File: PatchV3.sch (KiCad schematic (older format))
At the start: 28 parts, among them J1 Conn_01x05, J2 2908-05WB-MG, U1 STM32WB5MMGH6TR_1-

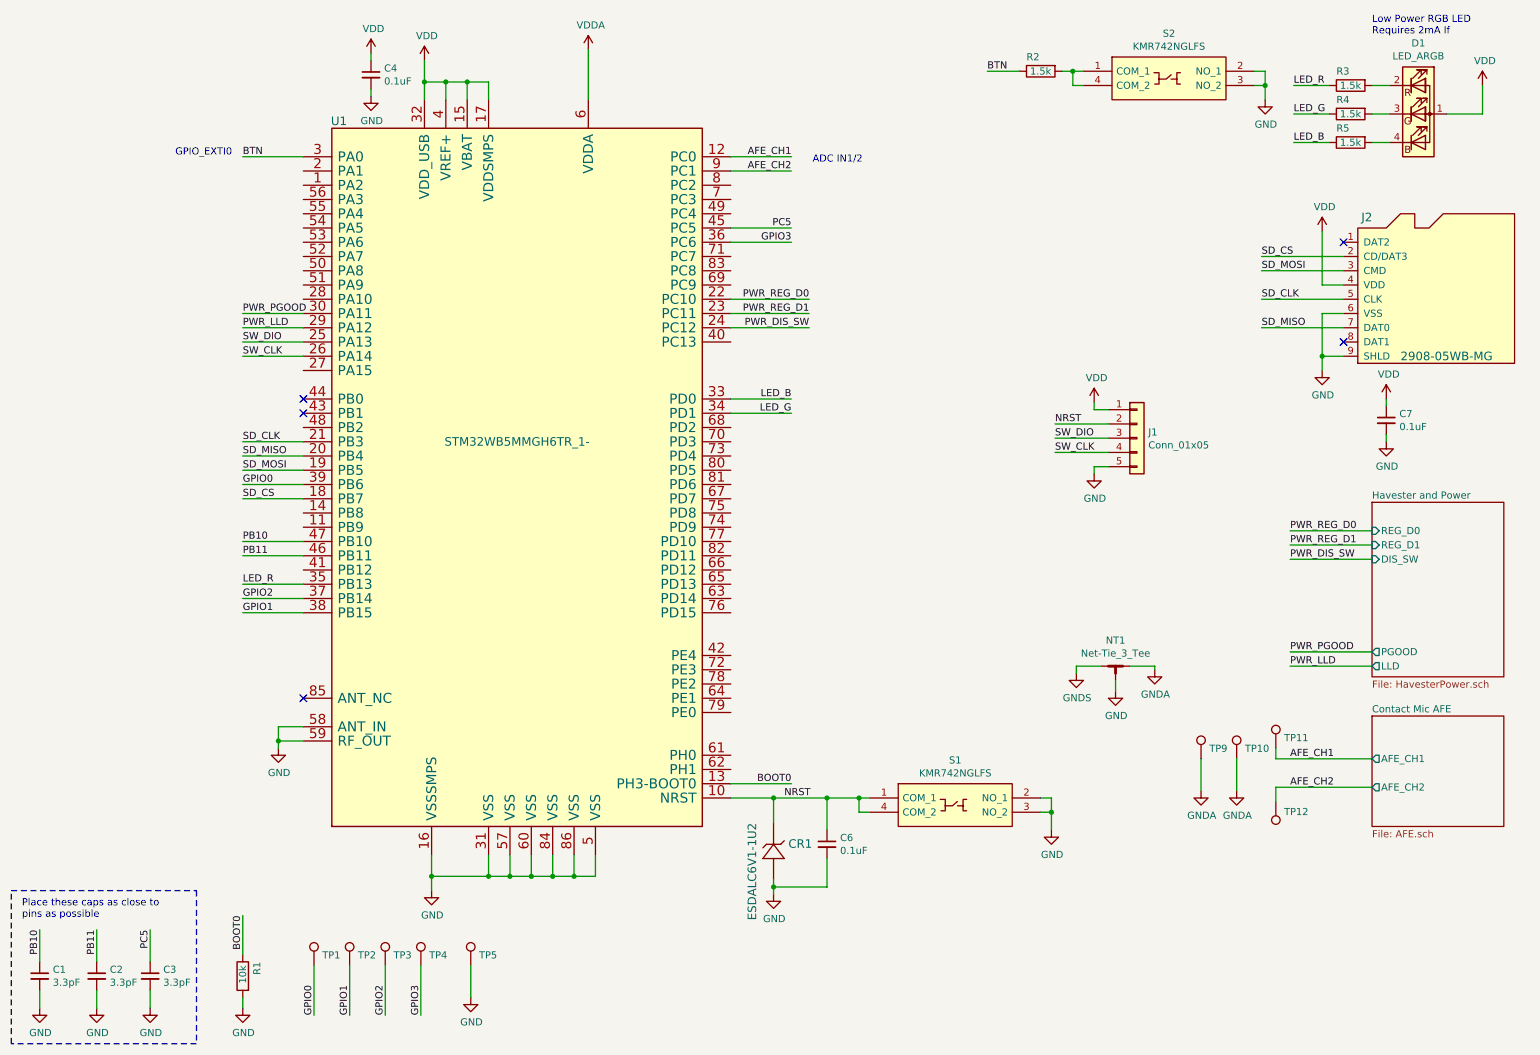
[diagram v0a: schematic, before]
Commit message: redid power section with new energy harverster ic
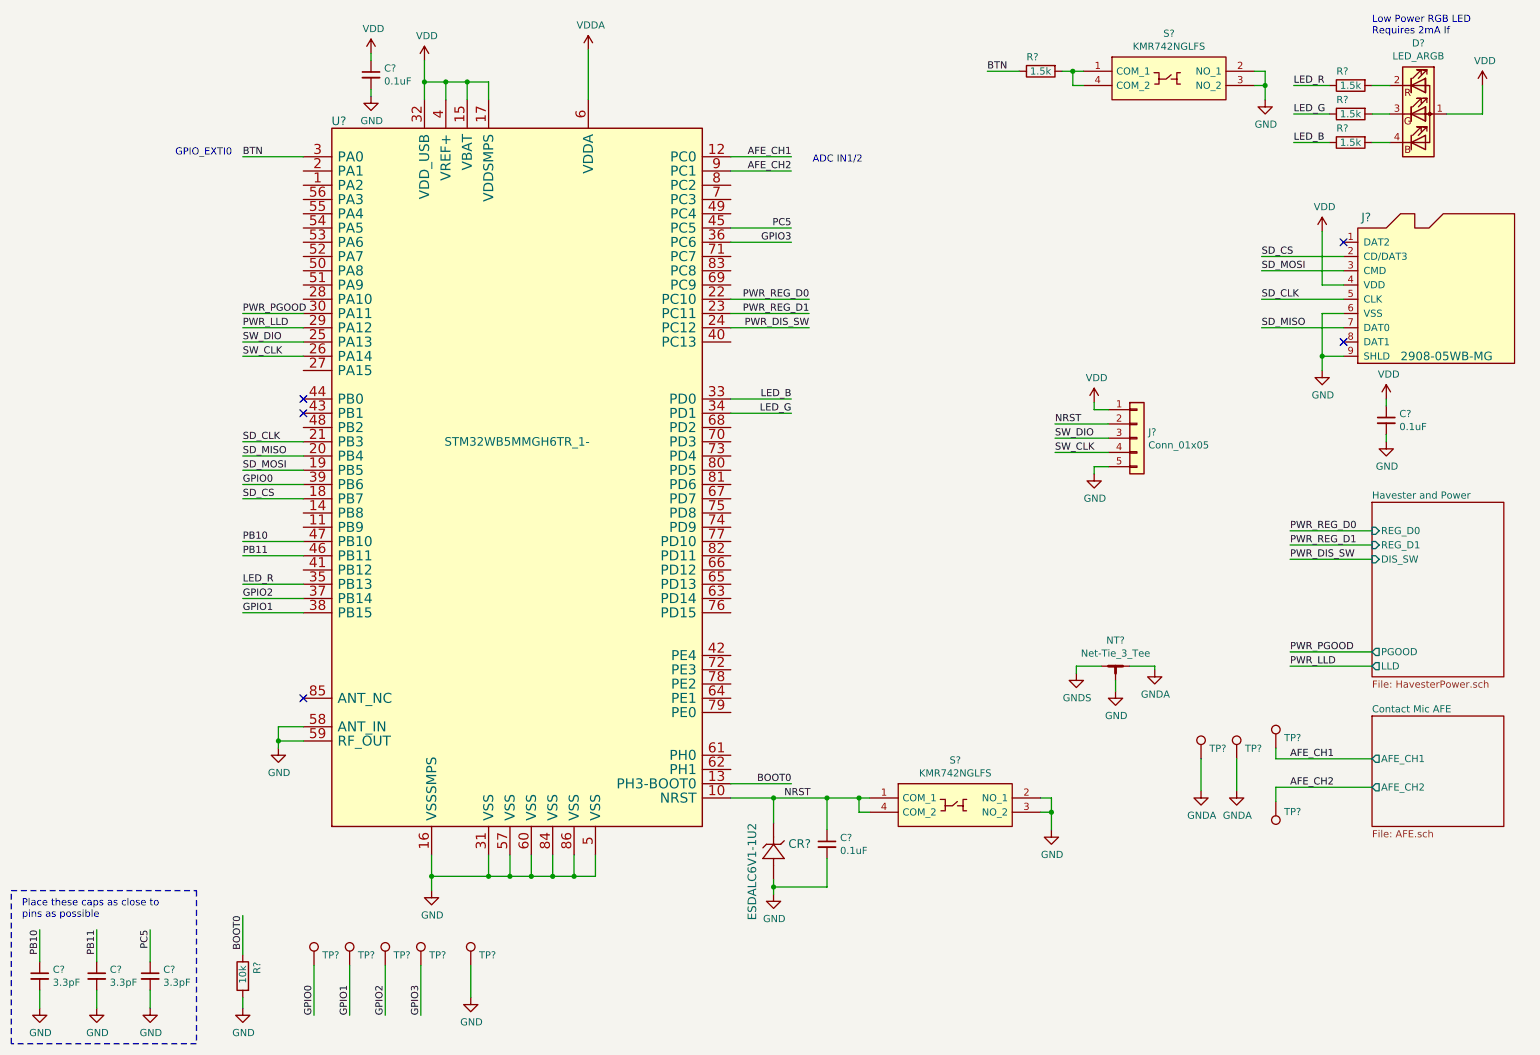
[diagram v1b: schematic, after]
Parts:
- renumbered C7 to C?, C6 to C?, C4 to C?, C1 to C?, C2 to C?, C3 to C?, CR1 to CR?, D1 to D?, J2 to J?, J1 to J?, NT1 to NT?, R3 to R?, R4 to R?, R5 to R?, R2 to R?, R1 to R?, S1 to S?, S2 to S?, TP1 to TP?, TP12 to TP?, TP2 to TP?, TP3 to TP?, TP4 to TP?, TP11 to TP?, TP5 to TP?, TP9 to TP?, TP10 to TP?, U1 to U?

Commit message: catch up
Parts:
- removed C? (x3): 3.3pF, Capacitor_SMD:C_0201_0603Metric, symbol Device:C_Small
- removed NT?: Net-Tie_3_Tee, PatchV2:gnd_tie, symbol Device:Net-Tie_3_Tee
- removed R?: 10k, Resistor_SMD:R_0402_1005Metric, symbol Device:R
- removed TP? (x4): TestPoint, TestPoint:TestPoint_Pad_1.5x1.5mm, symbol Connector:TestPoint
- removed U?: STM32WB5MMGH6TR_1-, PatchV2:SiP-LGA86, symbol PatchV2:STM32WB5MMGH6TR_1-
- added J?: Conn_02x04_Counter_Clockwise, symbol Connector_Generic:Conn_02x04_Counter_Clockwise
- added U?: LoRa-E5, PatchV2:LoRa-E5, symbol PatchV2:LoRa-E5
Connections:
- net labels added: LPUART_RX, LPUART_TX, ~BATT_CHG, ~BATT_CONN
- net labels removed: BOOT0, GNDS, PC5, VDDA
- wire segments 135 -> 109
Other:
- note added: "GPIO_EXTI5"
- note removed: "Place these caps as close to \npins as possible"
- moved on the sheet: C?, CR?, S?

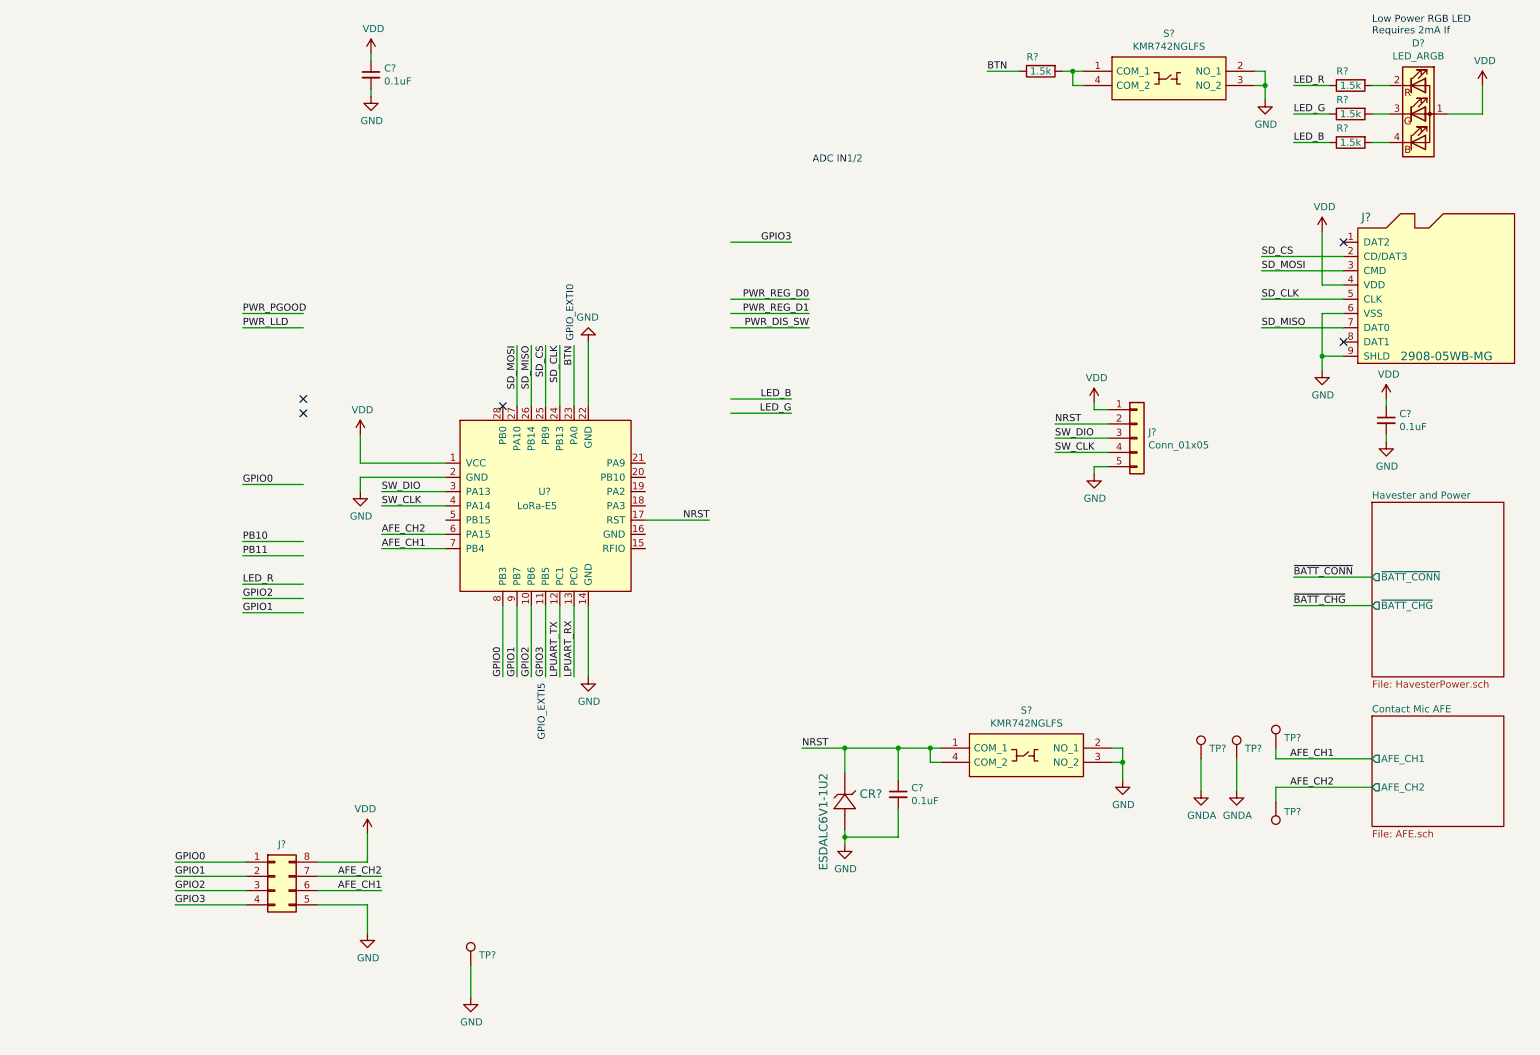
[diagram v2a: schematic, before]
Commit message: schematic functionally finished working on layout
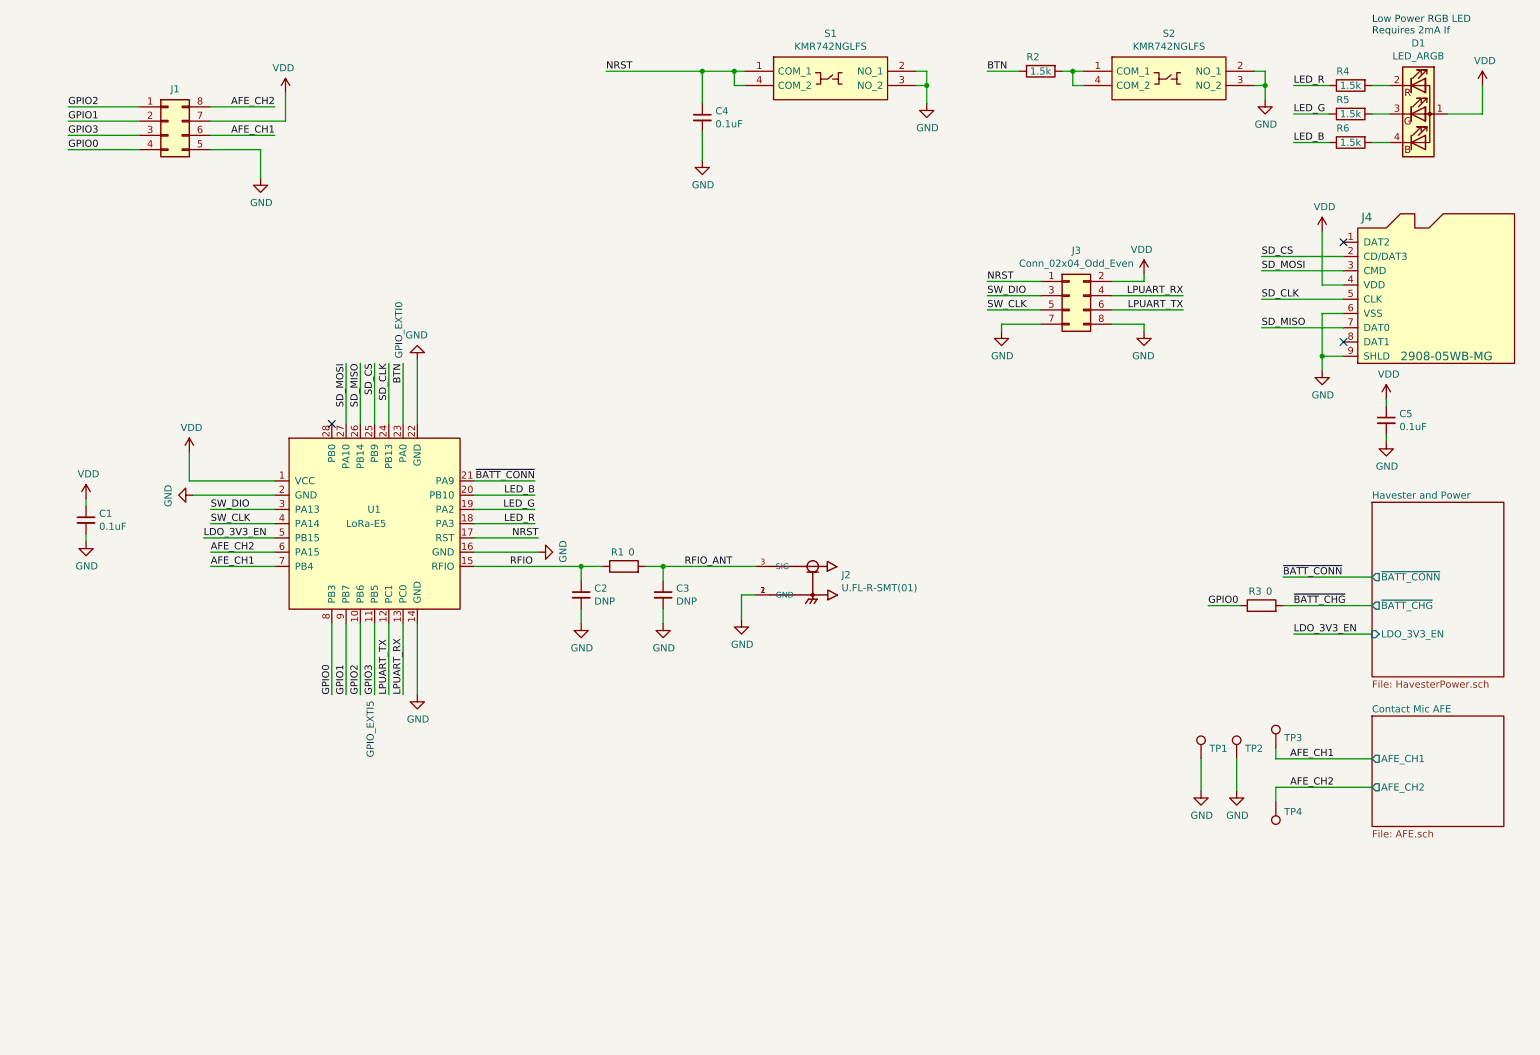
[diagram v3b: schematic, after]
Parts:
- removed CR?: ESDALC6V1-1U2, PatchV2:ESDALC6V1-1U2, symbol PatchV2:ESDALC6V1-1U2
- removed J?: Conn_01x05, Connector_PinHeader_2.54mm:PinHeader_1x05_P2.54mm_Horizontal, symbol Connector_Generic:Conn_01x05
- removed TP?: TestPoint, TestPoint:TestPoint_Pad_1.5x1.5mm, symbol Connector:TestPoint
- added C2, C3: DNP, Capacitor_SMD:C_0402_1005Metric, symbol Device:C_Small
- added J2: U.FL-R-SMT(01), PatchV2:HRS_U.FL-R-SMT(01), symbol PatchV2:U.FL-R-SMT(01)
- added J3: Conn_02x04_Odd_Even, Connector_PinHeader_2.54mm:PinHeader_2x04_P2.54mm_Horizontal, symbol Connector_Generic:Conn_02x04_Odd_Even
- added R1, R3: 0, Resistor_SMD:R_0402_1005Metric, symbol Device:R
- J1: renamed from J?; footprint (none) -> Connector_PinSocket_1.27mm:PinSocket_2x04_P1.27mm_Vertical
- gave numbers to parts that had none: 16
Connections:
- net labels added: LDO_3V3_EN, RFIO, RFIO_ANT
- net labels removed: GNDA, PB10, PB11, PWR_DIS_SW, PWR_LLD, PWR_PGOOD, PWR_REG_D0, PWR_REG_D1
- wire segments 109 -> 110
- no-connect marks 5 -> 3
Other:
- note removed: "ADC IN1/2\n"
- moved on the sheet: C1, C4, J1, S1, U1

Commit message: Finished pre-review layout
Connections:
- net AFE_CH1: now also J1.8 (Pin_8); no longer J1.6 (Pin_6)
- net AFE_CH2: now also J1.6 (Pin_6); no longer J1.8 (Pin_8)
- net LPUART_RX: now also J3.6 (Pin_6); no longer J3.4 (Pin_4)
- net LPUART_TX: now also J3.4 (Pin_4); no longer J3.6 (Pin_6)
- net NRST: now also J3.5 (Pin_5); no longer J3.1 (Pin_1)
- net SW_CLK: now also J3.1 (Pin_1); no longer J3.5 (Pin_5)
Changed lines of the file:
@@
 	8450 2375 8450 2425
 Wire Wire Line
-	7725 2425 7350 2425
+	7725 2625 7350 2625
 Wire Wire Line
 	7725 2525 7350 2525
-Text Label 7350 2425 0    50   ~ 0
+Text Label 7350 2625 0    50   ~ 0
 NRST
 Text Label 7350 2525 0    50   ~ 0
 SW_DIO
 Wire Wire Line
-	7725 2625 7350 2625
-Text Label 7350 2625 0    50   ~ 0
+	7725 2425 7350 2425
+Text Label 7350 2425 0    50   ~ 0
 SW_CLK
 Text Label 9425 4500 0    50   ~ 0
@@
 Wire Wire Line
 	1900 1500 2250 1500
+Text Label 2350 1200 2    50   ~ 0
+AFE_CH1
 Text Label 2350 1400 2    50   ~ 0
-AFE_CH1
-Text Label 2350 1200 2    50   ~ 0
 AFE_CH2
 Wire Wire Line
@@
 Wire Wire Line
 	8225 2425 8450 2425
+Text Label 8725 2525 2    50   ~ 0
+LPUART_TX
 Text Label 8725 2625 2    50   ~ 0
-LPUART_TX
-Text Label 8725 2525 2    50   ~ 0
 LPUART_RX
 Wire Wire Line
+	8225 2525 8725 2525
+Wire Wire Line
 	8225 2625 8725 2625
 Wire Wire Line
-	8225 2525 8725 2525
-Wire Wire Line
 	7450 2775 7450 2725
